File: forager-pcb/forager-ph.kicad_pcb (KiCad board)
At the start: 2 copper layers, 114.6 x 96.3 mm, 35 parts, among them J4 Conn_01x02_Pin

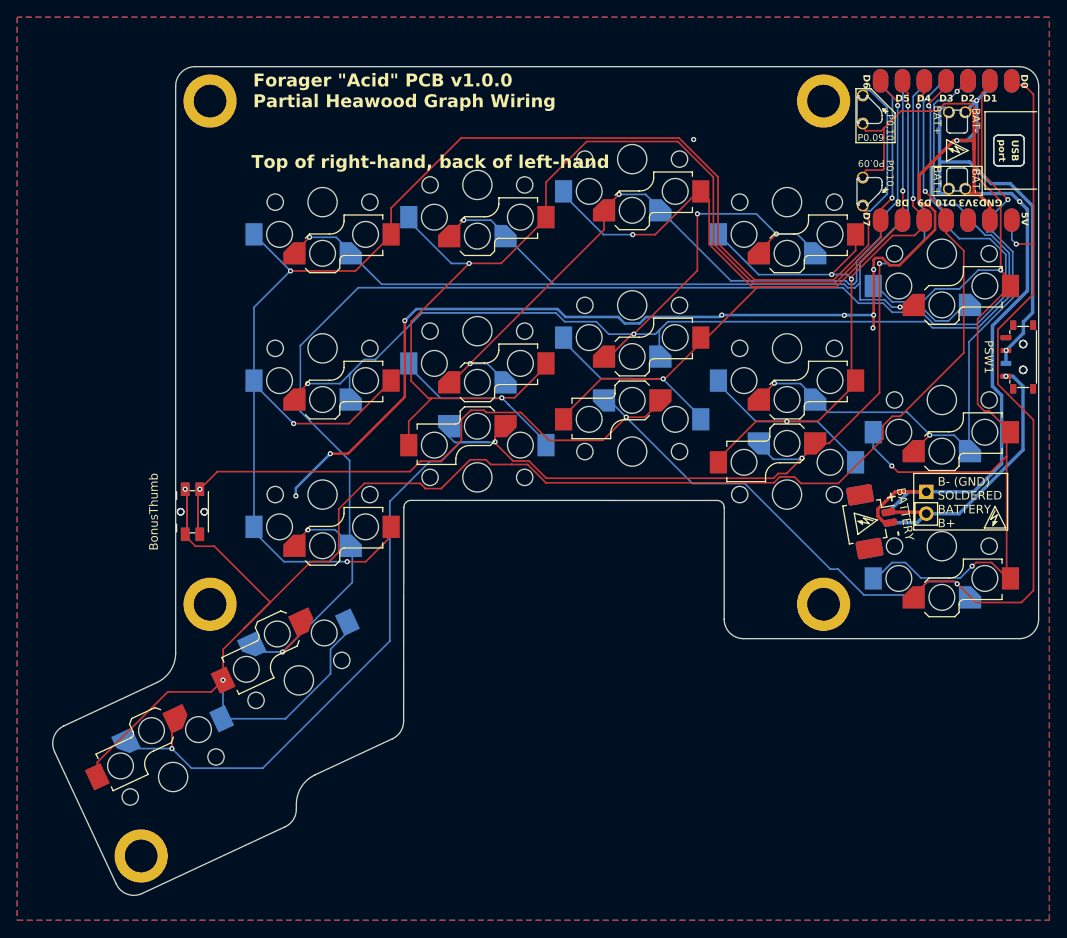
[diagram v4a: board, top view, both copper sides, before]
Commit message: Enlarge most 2x2.6mm hotswap pads to 2.6x2.6mm
This is more symetric and more closely matches the original Forager
hotswap footprint. Unclear why the Ceoloide Ergogen hotswaps are
that small on one side - although they work fined fine for me as is
on another board.

A few are still on the small side due to constaints like the battery
cut out, or wiring.
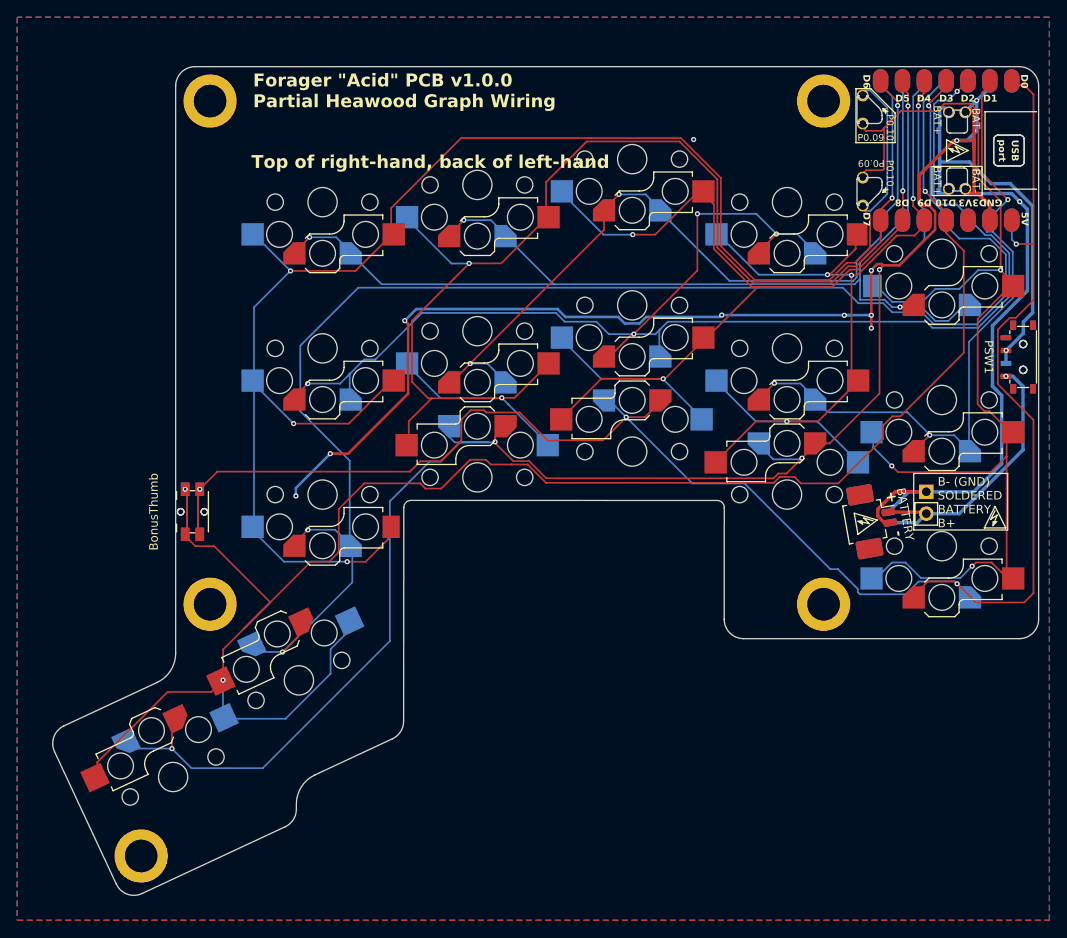
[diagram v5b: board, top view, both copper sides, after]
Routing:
- net GND: track 205.7 -> 204.8 mm
- net R4: track 209.5 -> 210.2 mm
- net R1: track 92.2 -> 91.5 mm
- net C0: track 186.7 -> 187.2 mm
- net R6: track 173.9 -> 173.4 mm
